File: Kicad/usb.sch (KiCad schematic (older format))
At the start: 21 parts, among them J501 USB Ports External, J502 USB Ports Internal, U501 MIC2005A-2YM5, U502 MIC2005A-2YM5, U503 XR22404CG28, U504 MIC2005A-2YM5, U505 MIC2005A-2YM5, Y501 12M

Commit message: Fix up ERC errors.
~FAULT on the MIC2005 is an active-low common collector output.
Well done ERC for spotting that I can't join three output pins together!
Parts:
- added R505: 10k, Resistor_SMD:R_0805_2012Metric_Pad1.15x1.40mm_HandSolder, symbol Device:R
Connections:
- wire segments 115 -> 116
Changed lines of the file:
@@
 L power:GND #PWR0515
 U 1 1 5FEB3B1E
-P 3650 4500
-F 0 "#PWR0515" H 3650 4250 50  0001 C CNN
-F 1 "GND" H 3655 4327 50  0000 C CNN
-F 2 "" H 3650 4500 50  0001 C CNN
-F 3 "" H 3650 4500 50  0001 C CNN
-	1    3650 4500
+P 3650 4850
+F 0 "#PWR0515" H 3650 4600 50  0001 C CNN
+F 1 "GND" H 3655 4677 50  0000 C CNN
+F 2 "" H 3650 4850 50  0001 C CNN
+F 3 "" H 3650 4850 50  0001 C CNN
+	1    3650 4850
 	-1   0    0    -1
 $EndComp
@@
 Wire Wire Line
 	9700 5400 9700 5350
+$Comp
+L Device:R R505
+U 1 1 5FE928D5
+P 3650 4650
+F 0 "R505" H 3700 4700 50  0000 L CNN
+F 1 "10k" H 3700 4600 50  0000 L CNN
+F 2 "Resistor_SMD:R_0805_2012Metric_Pad1.15x1.40mm_HandSolder" V 3580 4650 50  0001 C CNN
+F 3 "~" H 3650 4650 50  0001 C CNN
+	1    3650 4650
+	-1   0    0    -1
+$EndComp
+Wire Wire Line
+	3650 4800 3650 4850
 $EndSCHEMATC

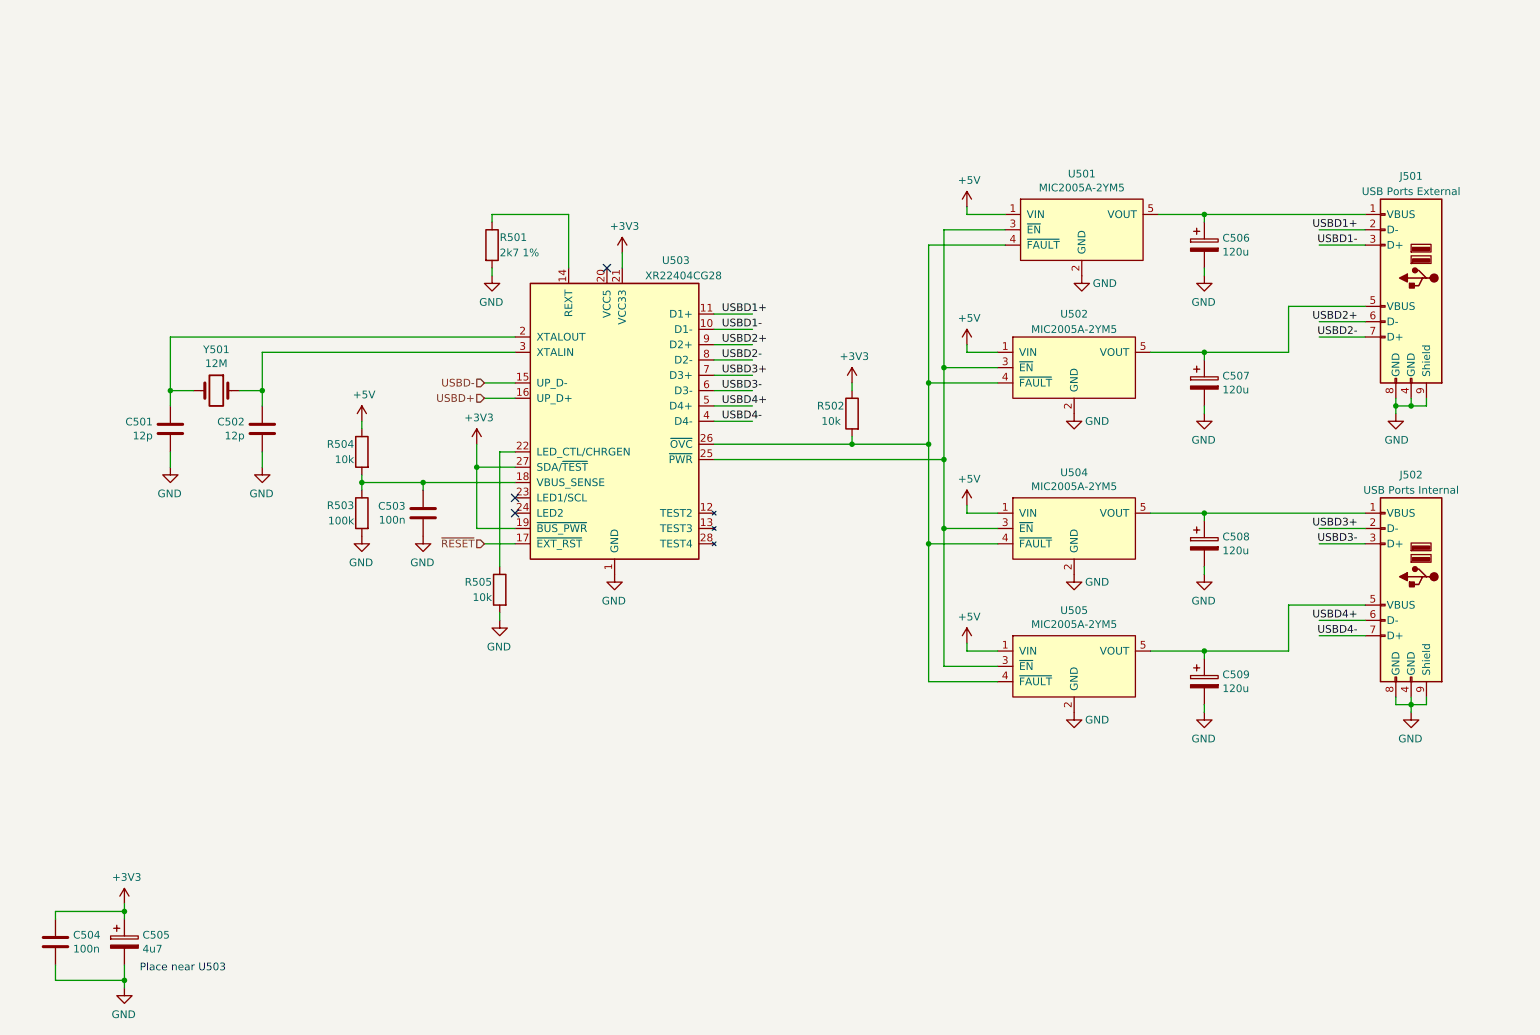
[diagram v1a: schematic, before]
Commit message: Added empty SD card sheet.
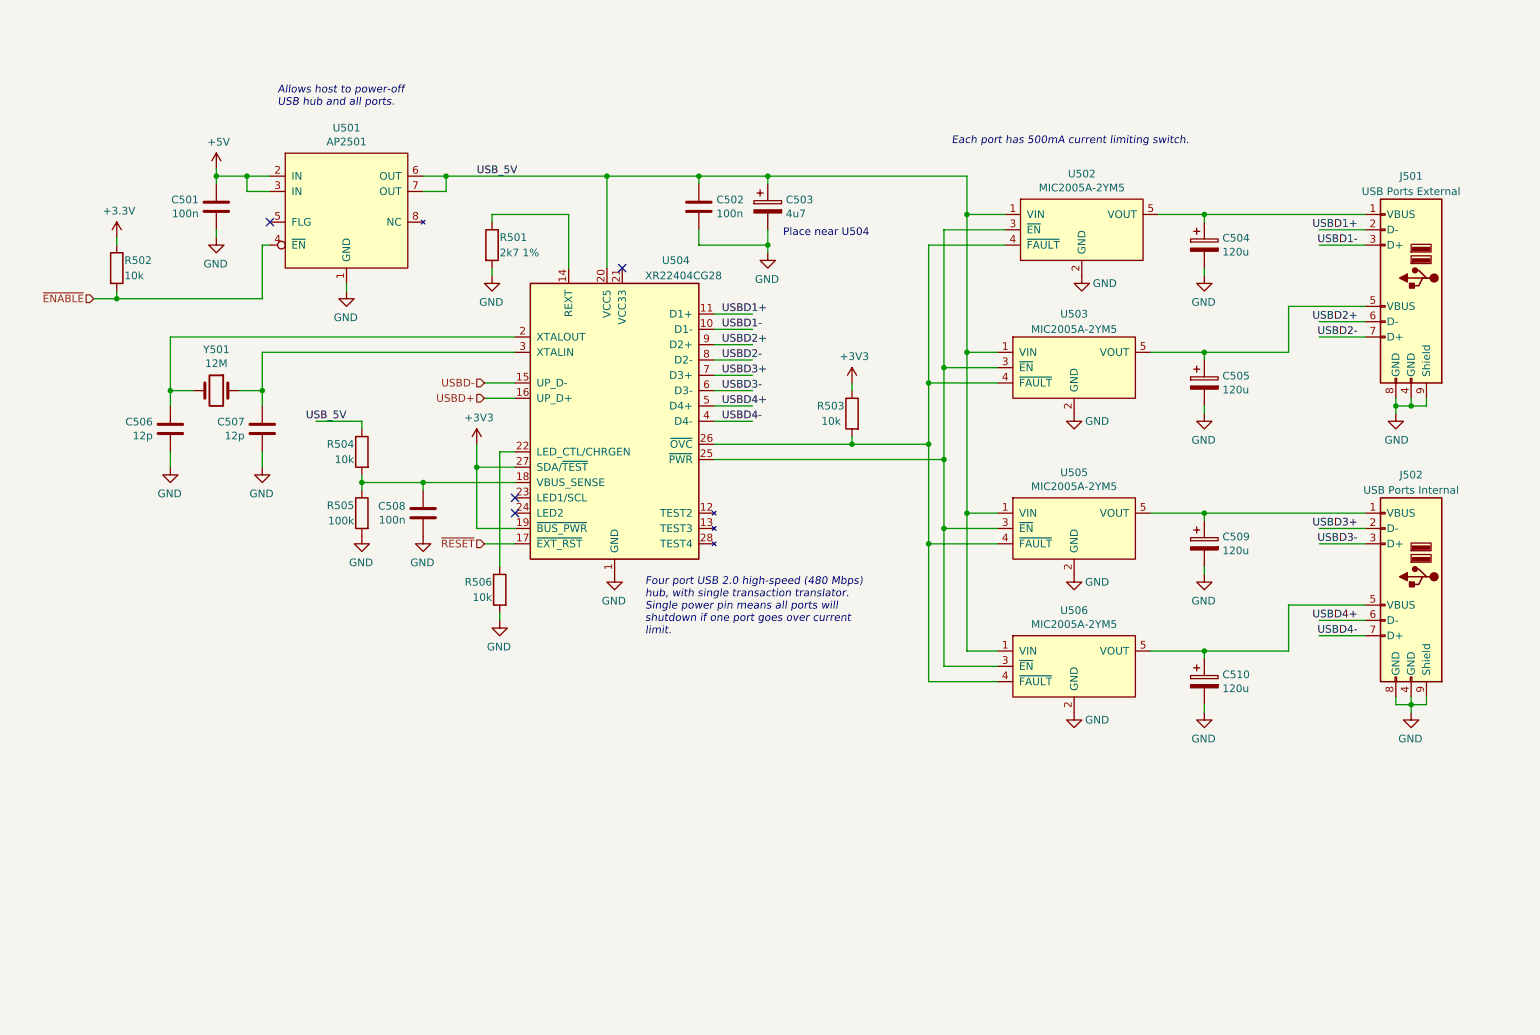
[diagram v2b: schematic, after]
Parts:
- added C501: 100n, Capacitor_SMD:C_0805_2012Metric_Pad1.15x1.40mm_HandSolder, symbol Device:C
- added R502: 10k, Resistor_SMD:R_0805_2012Metric_Pad1.15x1.40mm_HandSolder, symbol Device:R
- added U501: AP2501, Package_SO:SO-8_3.9x4.9mm_P1.27mm, symbol Neotron-Common-Hardware:AP2501
- renumbered C504 to C502, C505 to C503, C506 to C504, C507 to C505, C501 to C506, C502 to C507, C503 to C508, C508 to C509, C509 to C510, R502 to R503, R503 to R505, R505 to R506, U501 to U502, U502 to U503, U503 to U504, U504 to U505, U505 to U506
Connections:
- net labels added: +3.3V, USB_5V, ~ENABLE
- wire segments 116 -> 136
- no-connect marks 3 -> 4
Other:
- note added: "Allows host to power-off\nUSB hub and all ports."
- note added: "Each port has 500mA current limiting switch."
- note added: "Four port USB 2.0 high-speed (480 Mbps)\nhub, with single transaction translator.\nSingle power pin means all ports will\nshutdown if one port goes over current\nlimit."
- note added: "Place near U504"
- note removed: "Place near U503"
- moved on the sheet: C502, C503

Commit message: Replaced NUC029 (TSSOP) with KE04 (SOIC).
Also updated the BOM with some part nos.
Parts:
- C501, C502: DNP (none) -> 0; Digikey (none) -> BC1150CT-ND; MPN (none) -> K104K15X7RF5TL2; Manufacturer (none) -> Vishay
- C503, C504, C505, C509, C510, J501, J502, R501, R502, R503, R504, R505, R506: DNP (none) -> 0
- C508: Digikey (none) -> BC1150CT-ND; MPN (none) -> K104K15X7RF5TL2; Manufacturer (none) -> Vishay
- U501: DNP (none) -> 0; Digikey (none) -> AP2501S-13DICT-ND; MPN AP2501S-13 -> AP2501S-13
- U502, U503, U505, U506: DNP (none) -> 0; MPN (none) -> MIC2005A-2YM5; Manufacturer (none) -> Microchip
- U504: DNP (none) -> 0; Digikey (none) -> XR22404CG28TR-F-ND
- Y501: Digikey (none) -> 535-9037-ND; MPN (none) -> ABL-12.000MHZ-B2; Manufacturer (none) -> Abracon
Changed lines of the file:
@@
 F 5 "UJ2-ADH-1-TH" H 9600 4150 50  0001 C CNN "MPN"
 F 6 "102-4001-ND" H 9600 4050 50  0001 C CNN "Digikey"
+F 7 "0" H 9600 3000 50  0001 C CNN "DNP"
 	1    9600 3000
 	-1   0    0    -1
@@
 F 3 "http://www.microchip.com/mymicrochip/filehandler.aspx?ddocname=en579487" H 7450 2350 50  0001 C CNN
 F 4 "576-3464-1-ND" H 7450 2573 50  0001 C CNN "Digikey"
+F 5 "0" H 7450 2300 50  0001 C CNN "DNP"
+F 6 "MIC2005A-2YM5" H 7450 2300 50  0001 C CNN "MPN"
+F 7 "Microchip" H 7450 2300 50  0001 C CNN "Manufacturer"
 	1    7450 2300
 	1    0    0    -1
@@
 F 3 "http://www.microchip.com/mymicrochip/filehandler.aspx?ddocname=en579487" H 7400 3250 50  0001 C CNN
 F 4 "576-3464-1-ND" H 7400 3473 50  0001 C CNN "Digikey"
+F 5 "0" H 7400 3200 50  0001 C CNN "DNP"
+F 6 "MIC2005A-2YM5" H 7400 3200 50  0001 C CNN "MPN"
+F 7 "Microchip" H 7400 3200 50  0001 C CNN "Manufacturer"
 	1    7400 3200
 	1    0    0    -1
@@
 F 5 "XR22404CG28" H 4050 2500 50  0001 C CNN "MPN"
 F 6 "MaxLinear" H 4050 2600 50  0001 C CNN "Manufacturer"
+F 7 "0" H 4400 3550 50  0001 C CNN "DNP"
+F 8 "XR22404CG28TR-F-ND" H 4400 3550 50  0001 C CNN "Digikey"
 	1    4400 3550
 	1    0    0    -1
@@
 F 2 "Resistor_SMD:R_0805_2012Metric_Pad1.15x1.40mm_HandSolder" V 5880 3500 50  0001 C CNN
 F 3 "~" H 5950 3500 50  0001 C CNN
+F 4 "0" H 5950 3500 50  0001 C CNN "DNP"
 	1    5950 3500
 	-1   0    0    -1
@@
 F 3 "http://www.microchip.com/mymicrochip/filehandler.aspx?ddocname=en579487" H 7400 4300 50  0001 C CNN
 F 4 "576-3464-1-ND" H 7400 4523 50  0001 C CNN "Digikey"
+F 5 "0" H 7400 4250 50  0001 C CNN "DNP"
+F 6 "MIC2005A-2YM5" H 7400 4250 50  0001 C CNN "MPN"
+F 7 "Microchip" H 7400 4250 50  0001 C CNN "Manufacturer"
 	1    7400 4250
 	1    0    0    -1
@@
 F 3 "http://www.microchip.com/mymicrochip/filehandler.aspx?ddocname=en579487" H 7400 5200 50  0001 C CNN
 F 4 "576-3464-1-ND" H 7400 5423 50  0001 C CNN "Digikey"
+F 5 "0" H 7400 5150 50  0001 C CNN "DNP"
+F 6 "MIC2005A-2YM5" H 7400 5150 50  0001 C CNN "MPN"
+F 7 "Microchip" H 7400 5150 50  0001 C CNN "Manufacturer"
 	1    7400 5150
 	1    0    0    -1
@@
 F 3 "~" H 1800 3350 50  0001 C CNN
 F 4 "0" H 1800 3350 50  0001 C CNN "DNP"
+F 5 "535-9037-ND" H 1800 3350 50  0001 C CNN "Digikey"
+F 6 "ABL-12.000MHZ-B2" H 1800 3350 50  0001 C CNN "MPN"
+F 7 "Abracon" H 1800 3350 50  0001 C CNN "Manufacturer"
 	1    1800 3350
 	-1   0    0    -1
@@
 F 2 "Capacitor_THT:CP_Radial_D6.3mm_P2.50mm" H 5438 2000 50  0001 C CNN
 F 3 "~" H 5400 2150 50  0001 C CNN
+F 4 "0" H 5400 2150 50  0001 C CNN "DNP"
 	1    5400 2150
 	1    0    0    -1
@@
 F 2 "Capacitor_SMD:C_0805_2012Metric_Pad1.15x1.40mm_HandSolder" H 4988 2000 50  0001 C CNN
 F 3 "~" H 4950 2150 50  0001 C CNN
+F 4 "0" H 4950 2150 50  0001 C CNN "DNP"
+F 5 "BC1150CT-ND" H 4950 2150 50  0001 C CNN "Digikey"
+F 6 "K104K15X7RF5TL2" H 4950 2150 50  0001 C CNN "MPN"
+F 7 "Vishay" H 4950 2150 50  0001 C CNN "Manufacturer"
 	1    4950 2150
 	1    0    0    -1
@@
 F 3 "~" H 3150 4150 50  0001 C CNN
 F 4 "0" H 3150 4150 50  0001 C CNN "DNP"
+F 5 "BC1150CT-ND" H 3150 4150 50  0001 C CNN "Digikey"
+F 6 "K104K15X7RF5TL2" H 3150 4150 50  0001 C CNN "MPN"
+F 7 "Vishay" H 3150 4150 50  0001 C CNN "Manufacturer"
 	1    3150 4150
 	-1   0    0    -1
@@
 F 2 "Resistor_SMD:R_0805_2012Metric_Pad1.15x1.40mm_HandSolder" V 2680 4150 50  0001 C CNN
 F 3 "~" H 2750 4150 50  0001 C CNN
+F 4 "0" H 2750 4150 50  0001 C CNN "DNP"
 	1    2750 4150
 	-1   0    0    -1
@@
 F 2 "Resistor_SMD:R_0805_2012Metric_Pad1.15x1.40mm_HandSolder" V 3530 2400 50  0001 C CNN
 F 3 "~" H 3600 2400 50  0001 C CNN
+F 4 "0" H 3600 2400 50  0001 C CNN "DNP"
 	1    3600 2400
 	1    0    0    -1
@@
 F 2 "Capacitor_THT:CP_Radial_D6.3mm_P2.50mm" H 8288 2250 50  0001 C CNN
 F 3 "~" H 8250 2400 50  0001 C CNN
+F 4 "0" H 8250 2400 50  0001 C CNN "DNP"
 	1    8250 2400
 	1    0    0    -1
@@
 F 2 "Capacitor_THT:CP_Radial_D6.3mm_P2.50mm" H 8288 3150 50  0001 C CNN
 F 3 "~" H 8250 3300 50  0001 C CNN
+F 4 "0" H 8250 3300 50  0001 C CNN "DNP"
 	1    8250 3300
 	1    0    0    -1
@@
 F 2 "Capacitor_THT:CP_Radial_D6.3mm_P2.50mm" H 8288 4200 50  0001 C CNN
 F 3 "~" H 8250 4350 50  0001 C CNN
+F 4 "0" H 8250 4350 50  0001 C CNN "DNP"
 	1    8250 4350
 	1    0    0    -1
@@
 F 2 "Capacitor_THT:CP_Radial_D6.3mm_P2.50mm" H 8288 5100 50  0001 C CNN
 F 3 "~" H 8250 5250 50  0001 C CNN
+F 4 "0" H 8250 5250 50  0001 C CNN "DNP"
 	1    8250 5250
 	1    0    0    -1
@@
 F 2 "Resistor_SMD:R_0805_2012Metric_Pad1.15x1.40mm_HandSolder" V 2680 3750 50  0001 C CNN
 F 3 "~" H 2750 3750 50  0001 C CNN
+F 4 "0" H 2750 3750 50  0001 C CNN "DNP"
 	1    2750 3750
 	-1   0    0    -1
@@
 F 1 "USB Ports Internal" H 9600 5900 50  0000 C CNN
 F 2 "Neotron-Common-Hardware:USB_Header" H 9550 6200 50  0001 C CNN
-F 3 "" H 9750 5000 50  0001 C CNN
+F 3 "~" H 9750 5000 50  0001 C CNN
+F 4 "0" H 9600 4950 50  0001 C CNN "DNP"
 	1    9600 4950
 	-1   0    0    -1
@@
 F 2 "Resistor_SMD:R_0805_2012Metric_Pad1.15x1.40mm_HandSolder" V 3580 4650 50  0001 C CNN
 F 3 "~" H 3650 4650 50  0001 C CNN
+F 4 "0" H 3650 4650 50  0001 C CNN "DNP"
 	1    3650 4650
 	-1   0    0    -1
@@
 F 3 "https://www.diodes.com/assets/Datasheets/AP25x1.pdf" H 2650 1200 50  0001 C CNN
 F 4 "Diodes Incorporated" H 2650 1050 50  0001 C CNN "Manufacturer"
-F 5 " AP2501S-13" H 2600 950 50  0001 C CNN "MPN"
+F 5 "AP2501S-13" H 2600 950 50  0001 C CNN "MPN"
+F 6 "0" H 2650 1200 50  0001 C CNN "DNP"
+F 7 "AP2501S-13DICT-ND" H 2650 1200 50  0001 C CNN "Digikey"
 	1    2650 1200
 	1    0    0    -1
@@
 F 2 "Resistor_SMD:R_0805_2012Metric_Pad1.15x1.40mm_HandSolder" V 1080 2550 50  0001 C CNN
 F 3 "~" H 1150 2550 50  0001 C CNN
+F 4 "0" H 1150 2550 50  0001 C CNN "DNP"
 	1    1150 2550
 	1    0    0    -1
@@
 F 2 "Capacitor_SMD:C_0805_2012Metric_Pad1.15x1.40mm_HandSolder" H 1838 2000 50  0001 C CNN
 F 3 "~" H 1800 2150 50  0001 C CNN
+F 4 "0" H 1800 2150 50  0001 C CNN "DNP"
+F 5 "BC1150CT-ND" H 1800 2150 50  0001 C CNN "Digikey"
+F 6 "K104K15X7RF5TL2" H 1800 2150 50  0001 C CNN "MPN"
+F 7 "Vishay" H 1800 2150 50  0001 C CNN "Manufacturer"
 	1    1800 2150
 	-1   0    0    -1
